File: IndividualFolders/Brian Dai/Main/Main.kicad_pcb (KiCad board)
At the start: 4 copper layers, 76.2 x 67.6 mm, 77 parts, among them J1 USB_B_Micro, J3 Conn_01x03, J4 Conn_01x03, J5 Conn_01x03, J6 Conn_01x03, SW1 SW_Push, SW2 SW_Push, U1 RP2350A-QFN60, U10 LM75B, U11 MCS1802GS-50-Z, U12 MCS1802GS-50-Z, U13 MCS1802GS-50-Z, U14 LM2575-3.3BT, U2 W25Q128JVS, U3 AMS1117-3.3, U4 MMC5983MA, U5 ICM-42688-P, U6 INA226, U7 KX134-1211, U8 MS5611-01BA, U9 MCS1802GS-50-Z, Y1 ABM8-272-T3

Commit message: .
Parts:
- moved J6 21.9 mm to (132.3, 91.0), turned to 180 degrees
- moved U12 16.4 mm to (127.2, 89.4), turned to 90 degrees
- moved U11 13.1 mm to (128.2, 98.6)
- moved U14 12.6 mm to (116.2, 84.7)
- moved J3 10.00 mm to (133.5, 100.5)
- moved U13 9.08 mm to (128.8, 107.4)
- moved J4 9.02 mm to (128.0, 114.4)
- moved J5 8.73 mm to (133.5, 104.9)
- moved U6 7.71 mm to (111.5, 96.0)
- moved U9 7.38 mm to (122.8, 117.1)

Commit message: Meeting 2/28/26
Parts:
- removed U14: LM2575-3.3BT, Package_TO_SOT_SMD:TO-263-5_TabPin3
- added C37: 10u, Capacitor_SMD:C_0805_2012Metric, F.Cu at (106.5, 118.0)
- added C38: 100n, Capacitor_SMD:C_0402_1005Metric, F.Cu at (104.2, 118.0)
- added C39: 10u, Capacitor_SMD:C_0805_2012Metric, F.Cu at (65.8, 103.5)
- added C40: 100n, Capacitor_SMD:C_0402_1005Metric, F.Cu at (72.0, 100.8)
- added C41: 22u, Capacitor_SMD:C_0805_2012Metric, F.Cu at (65.8, 100.0)
- added J2: XT60, Connector_AMASS:AMASS_XT60-M_1x02_P7.20mm_Vertical, F.Cu at (85.0, 129.0)
- added J7: MSD-4-A, otherComponents:CUI_MSD-4-A, B.Cu at (100.0, 125.3)
- added J9: Conn_01x03, Connector_PinHeader_2.54mm:PinHeader_1x03_P2.54mm_Vertical, F.Cu at (118.0, 116.0)
- added L3: 3.3u, Inductor_SMD:L_1008_2520Metric_Pad1.43x2.20mm_HandSolder, F.Cu at (69.2, 99.0)
- added Q2: Si2301CDS, Package_TO_SOT_SMD:SOT-23, F.Cu at (79.0, 100.0)
- added R14: 10k, Resistor_SMD:R_0402_1005Metric, F.Cu at (99.5, 120.8)
- added R15: 10k, Resistor_SMD:R_0402_1005Metric, F.Cu at (106.5, 120.8)
- added R16: 10k, Resistor_SMD:R_0402_1005Metric, F.Cu at (104.5, 120.8)
- added R17: 10k, Resistor_SMD:R_0402_1005Metric, F.Cu at (100.5, 120.8)
- added R18: 10k, Resistor_SMD:R_0402_1005Metric, F.Cu at (101.5, 120.8)
- added R20: 30k, Resistor_SMD:R_0603_1608Metric, F.Cu at (75.0, 103.2)
- added R21: 10k, Resistor_SMD:R_0402_1005Metric, F.Cu at (71.5, 104.8)
- added R22: 100k, Resistor_SMD:R_0402_1005Metric, F.Cu at (81.0, 102.0)
- added R23: 1k, Resistor_SMD:R_0402_1005Metric, F.Cu at (72.5, 103.2)
- added R9: 10k, Resistor_SMD:R_0402_1005Metric, F.Cu at (105.5, 120.8)
- added U15: AP62150WU, Package_TO_SOT_SMD:TSOT-23-6, F.Cu at (69.2, 102.5)
- D1: value LED -> RED_LED
- D2: value LED -> BLUE_LED
- D3: value LED -> GREEN_LED
- moved C20 126.6 mm to (116.5, 130.8), turned to 180 degrees
- moved C21 122.0 mm to (113.0, 130.8), turned to 180 degrees
- moved C22 120.5 mm to (132.9, 108.0), turned to 180 degrees
- moved C23 120.3 mm to (131.5, 101.0)
- moved C19 110.5 mm to (103.2, 118.0), turned to -90 degrees
- moved R5 109.8 mm to (107.0, 125.0)
- moved C27 109.8 mm to (132.0, 93.0), turned to 90 degrees
- moved C30 108.8 mm to (113.8, 111.2), turned to 180 degrees
- moved C11 107.8 mm to (101.8, 105.6), turned to -45 degrees
- moved C29 107.7 mm to (109.5, 110.5), turned to -90 degrees
- moved C26 104.6 mm to (119.8, 99.5), turned to -90 degrees
- moved C25 103.6 mm to (115.8, 100.0), turned to -90 degrees
- moved C13 102.4 mm to (106.8, 98.2), turned to 45 degrees
- moved R4 101.5 mm to (93.0, 125.0)
- moved C15 101.0 mm to (105.5, 103.5), turned to -45 degrees
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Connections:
- C29 pad 2: Net-(C29-Pad2) -> GND
- C30 pad 2: Net-(C29-Pad2) -> GND
- R13 pad 1: GND -> VIN
- R13 pad 2: VSS -> Net-(J2-Pin_2)
- U1 pad 24: unconnected-(U1-SWCLK-Pad24) -> Net-(J9-Pin_3)
- U1 pad 25: unconnected-(U1-SWDIO-Pad25) -> Net-(J9-Pin_2)
- U1 pad 32: unconnected-(U1-GPIO20-Pad32) -> SDA
- U1 pad 33: unconnected-(U1-GPIO21-Pad33) -> SCL
- U1 pad 40: unconnected-(U1-GPIO26_ADC0-Pad40) -> Vout1
- U1 pad 41: unconnected-(U1-GPIO27_ADC1-Pad41) -> Vout2
- U1 pad 42: unconnected-(U1-GPIO28_ADC2-Pad42) -> Vout4
- U1 pad 43: unconnected-(U1-GPIO29_ADC3-Pad43) -> Vout3
- U11 pad 1: current + -> VIN
- U11 pad 2: current + -> VIN
- U12 pad 3: current + -> VIN
- U12 pad 4: current + -> VIN
- U13 pad 1: current + -> VIN
- U13 pad 2: current + -> VIN
- U6 pad 10: VSS -> Net-(J2-Pin_2)
- U6 pad 8: GND -> Net-(J2-Pin_2)
- U6 pad 9: GND -> VIN
- U7 pad 1: ACCEL_SDO/ADDR -> SPI_SD0
- U7 pad 2: ACCEL_SDI/SDA -> SPI_SDI
- U9 pad 3: current + -> VIN
- U9 pad 4: current + -> VIN
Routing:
- net GND: track 0.18 -> 105.7 mm, vias 2 -> 55
- net +3.3V: track 12.1 -> 104.9 mm, vias 0 -> 27
- net SCL: track 0.00 -> 61.0 mm, vias 0 -> 3
- net VBUS: track 0.00 -> 56.0 mm, vias 0 -> 9
- net SDA: track 0.00 -> 48.2 mm, vias 0 -> 3
- net Vout1: track 0.00 -> 34.6 mm
- net Net-(U1-RUN): track 0.00 -> 31.4 mm, vias 0 -> 2
- net +1V1: track 4.52 -> 34.6 mm
- net /USB_D-: track 0.00 -> 27.6 mm
- net /USB_D+: track 0.00 -> 27.0 mm
- net Vout2: track 0.00 -> 22.1 mm
- net /QSPI_SS: track 7.25 -> 27.3 mm
- net Vout3: track 0.00 -> 19.5 mm
- net Vout4: track 0.00 -> 17.5 mm
- net Net-(U1-XIN): track 0.00 -> 10.3 mm
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- added copper zone on F.Cu, net +3.3V
- added copper zone on In2.Cu, net +3.3V
- added copper zone on F.Cu, net GND
- added copper zone on In1.Cu, net GND
- added copper zone on F.Cu, net Net-(J2-Pin_2)
- added copper zone on F.Cu, net Net-(Q2-S)
- added copper zone on F.Cu, net Net-(U15-BST)
- added copper zone on F.Cu, net Net-(U15-FB)
- added copper zone on F.Cu, net Net-(U15-SW)
- added copper zone on F.Cu, net VBUS
- added copper zone on In2.Cu, net VBUS
- added copper zone on F.Cu, net VIN
- added copper zone on In2.Cu, net VIN
- added copper zone on F.Cu, net current -4
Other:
- board size 76.2 x 67.6 mm -> 76.2 x 64.9 mm
- board text added: "SIG, GND, PWR, SIG Stackup"

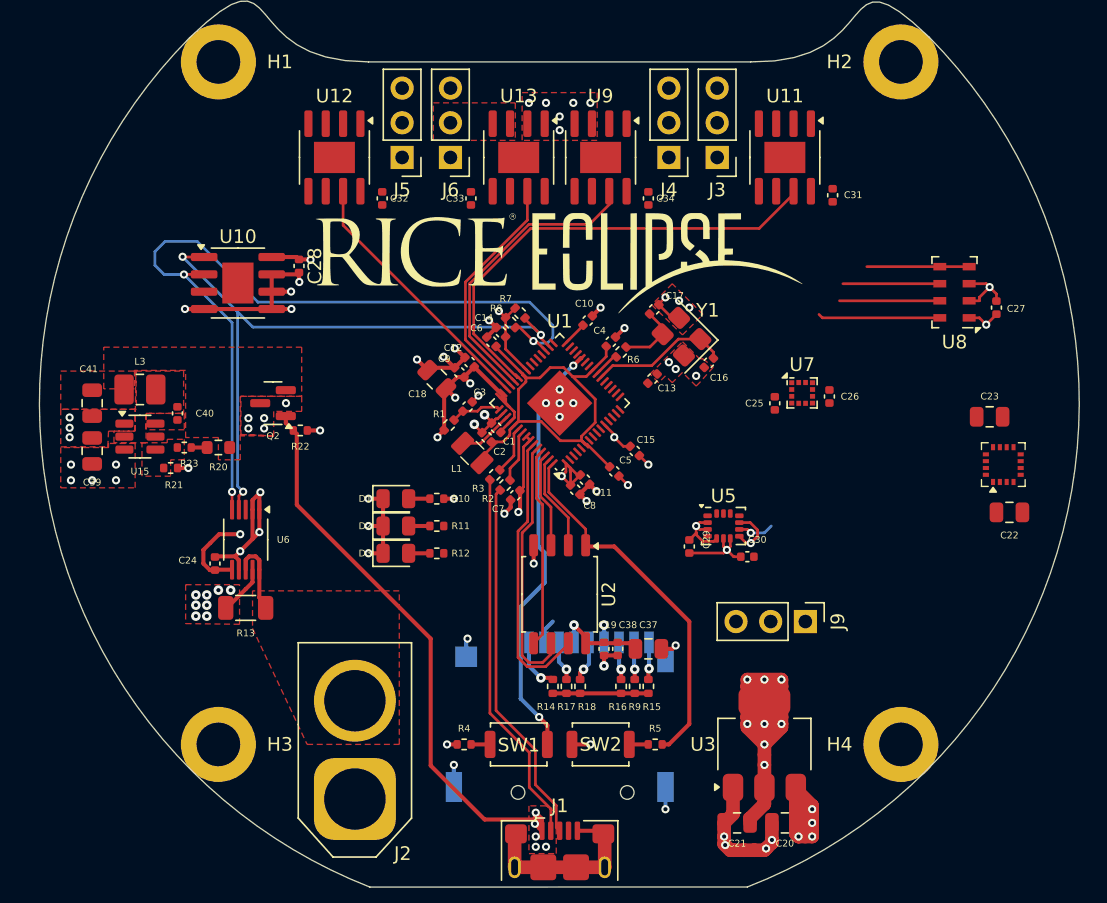
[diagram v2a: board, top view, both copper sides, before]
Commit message: Resistor component numbers
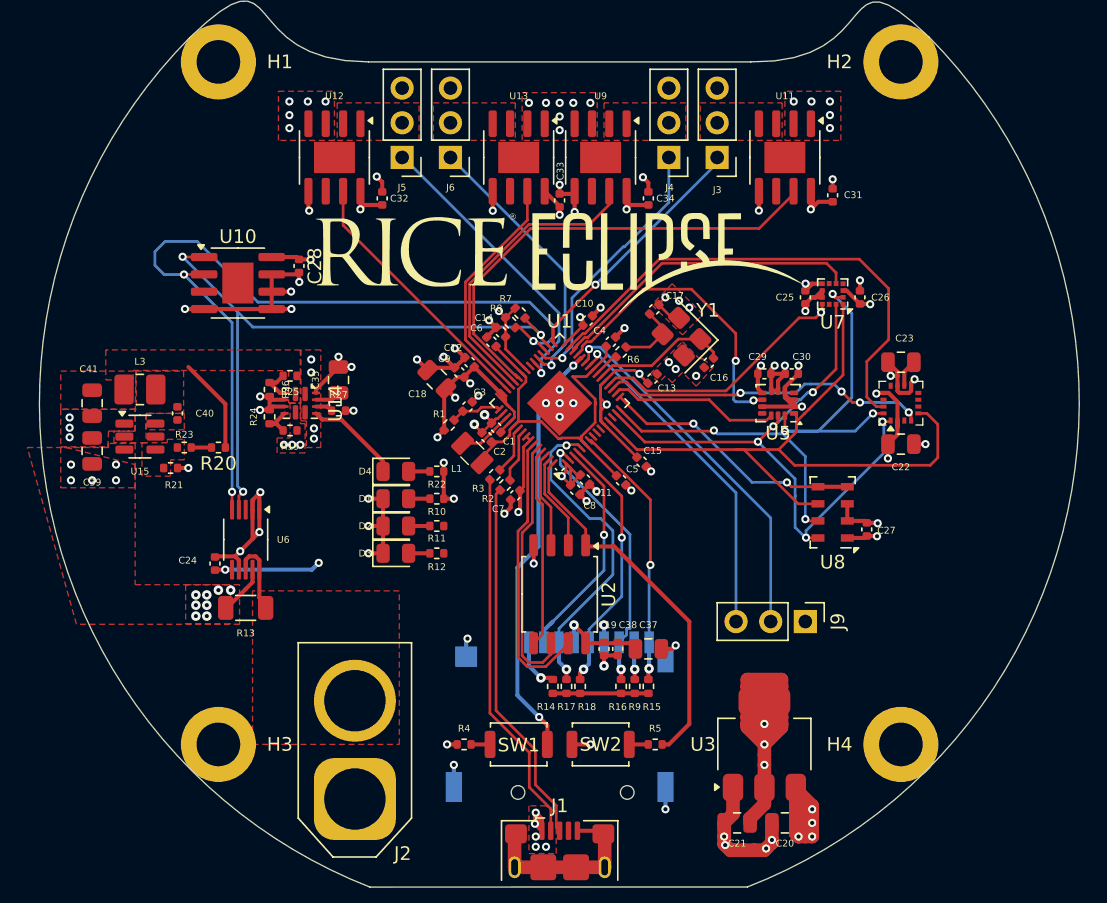
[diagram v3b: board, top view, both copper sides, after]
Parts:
- removed Q2: Si2301CDS, Package_TO_SOT_SMD:SOT-23
- added C35: 1u, Capacitor_SMD:C_0805_2012Metric, F.Cu at (83.8, 98.3)
- added D4: RED_LED, LED_SMD:LED_0805_2012Metric, F.Cu at (88.0, 105.0)
- added R19: 30k, Resistor_SMD:R_0402_1005Metric, F.Cu at (80.2, 102.0)
- added R24: 100k, Resistor_SMD:R_0402_1005Metric, F.Cu at (78.8, 101.0)
- added R25: 100k, Resistor_SMD:R_0402_1005Metric, F.Cu at (80.2, 98.0)
- added R26: 100k, Resistor_SMD:R_0402_1005Metric, F.Cu at (78.8, 99.0)
- added R27: 100k, Resistor_SMD:R_0402_1005Metric, F.Cu at (83.8, 100.5)
- added U14: TPS2121RUXR, Package_DFN_QFN:Texas_VQFN-HR-12_2x2.5mm_P0.5mm, F.Cu at (81.0, 100.0)
- D2: value BLUE_LED -> YELLOW_LED
- R10: value R -> 60
- R20: footprint Resistor_SMD:R_0603_1608Metric -> Resistor_SMD:R_0402_1005Metric
- R22: value 100k -> 60
- moved C27 18.8 mm to (122.5, 109.2)
- moved U8 18.4 mm to (120.0, 108.0)
- moved C29 13.8 mm to (115.0, 97.8), turned to 0 degrees
- moved C30 13.8 mm to (117.0, 97.8)
- moved R22 10.4 mm to (91.0, 105.0)
- moved U5 9.85 mm to (116.0, 100.0), turned to 180 degrees
- moved C22 9.39 mm to (125.0, 103.0)
- moved U4 8.75 mm to (125.0, 100.0)
- moved C25 8.08 mm to (118.0, 92.2)
- moved C23 7.63 mm to (125.0, 97.0), turned to 180 degrees
- moved C26 7.60 mm to (122.0, 92.2)
- moved U7 7.59 mm to (120.0, 92.0), turned to 180 degrees
- moved C33 6.50 mm to (100.0, 85.2)
- moved C15 0.94 mm to (106.0, 104.3)
- moved C5 0.82 mm to (104.5, 105.7)
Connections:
- net Net-(Q2-S) renamed 3.3v_Batt
- C21 pad 1: +3.3V -> 3.3v_usb
- C25 pad 1: IO_VDD -> +3.3V
- C26 pad 2: VDD -> +3.3V
- R22 pad 1: GND -> +3.3V
- R22 pad 2: VBUS -> Net-(D4-A)
- U1 pad 12: unconnected-(U1-GPIO8-Pad12) -> SPI_SDO
- U1 pad 14: unconnected-(U1-GPIO10-Pad14) -> SPI_SCK
- U1 pad 15: unconnected-(U1-GPIO11-Pad15) -> SPI_SDI
- U1 pad 16: unconnected-(U1-GPIO12-Pad16) -> MS5611_CS
- U1 pad 17: unconnected-(U1-GPIO13-Pad17) -> ICM_CS
- U1 pad 18: unconnected-(U1-GPIO14-Pad18) -> MMC_CS
- U1 pad 19: unconnected-(U1-GPIO15-Pad19) -> ACCEL_CS
- U1 pad 2: unconnected-(U1-GPIO0-Pad2) -> SPI_SDO2
- U1 pad 27: unconnected-(U1-GPIO16-Pad27) -> INT2/DRDY
- U1 pad 28: unconnected-(U1-GPIO17-Pad28) -> ACCEL_INT
- U1 pad 29: unconnected-(U1-GPIO18-Pad29) -> MMC_INT
- U1 pad 3: unconnected-(U1-GPIO1-Pad3) -> SD_ChipSelect
- U1 pad 31: unconnected-(U1-GPIO19-Pad31) -> PWM1
- U1 pad 34: unconnected-(U1-GPIO22-Pad34) -> PWM2
- U1 pad 35: unconnected-(U1-GPIO23-Pad35) -> PWM4
- U1 pad 36: unconnected-(U1-GPIO24-Pad36) -> PWM3
- U1 pad 4: unconnected-(U1-GPIO2-Pad4) -> SPI_SCLK2
- U1 pad 5: unconnected-(U1-GPIO3-Pad5) -> SPI_SDI2
- U1 pad 7: unconnected-(U1-GPIO4-Pad7) -> SD_CD
- U3 pad 2: +3.3V -> 3.3v_usb
- U4 pad 15: unconnected-(U4-INT-Pad15) -> MMC_INT
- U4 pad 5: SPI_SD0 -> SPI_SDO
- U5 pad 1: SPI_SD0 -> SPI_SDO
- U7 pad 1: SPI_SD0 -> SPI_SDO
- U7 pad 10: ACCEL_nCS -> ACCEL_CS
- U7 pad 3: IO_VDD -> +3.3V
- U7 pad 5: ACCEL_INT1 -> ACCEL_INT
- U7 pad 6: ACCEL_INT2 -> unconnected-(U7-INT2-Pad6)
- U7 pad 7: VDD -> +3.3V
- U8 pad 6: SDO -> SPI_SDO
- U8 pad 7: SDI -> SPI_SDI
- U8 pad 8: SCLK -> SPI_SCK
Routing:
- net SPI_SDO: track 0.00 -> 51.6 mm
- net SPI_SCK: track 0.00 -> 45.8 mm, vias 0 -> 5
- net SPI_SDI: track 0.00 -> 44.9 mm, vias 0 -> 5
- net VBUS: track 56.0 -> 16.7 mm
- net MMC_INT: track 0.00 -> 37.0 mm
- net 3.3v_usb: track 0.00 -> 29.9 mm, vias 0 -> 6
- net GND: track 105.7 -> 133.6 mm, vias 55 -> 73
- net Net-(J9-Pin_2): track 0.00 -> 27.2 mm, vias 0 -> 1
- net Net-(J9-Pin_3): track 0.00 -> 24.9 mm, vias 0 -> 1
- net MMC_CS: track 0.00 -> 24.2 mm, vias 0 -> 4
- net ACCEL_INT: track 0.00 -> 23.0 mm
- net PWM3: track 0.00 -> 22.2 mm, vias 0 -> 1
- net SPI_SDI2: track 2.95 -> 23.3 mm, vias 1 -> 2
- net PWM4: track 0.00 -> 20.3 mm, vias 0 -> 1
- net PWM2: track 0.00 -> 19.7 mm, vias 0 -> 1
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- added copper zone on F.Cu, net 3.3v_usb
- added copper zone on In2.Cu, net 3.3v_usb
- added copper zone on F.Cu, net current -1
- added copper zone on F.Cu, net current -2
- added copper zone on F.Cu, net current -3
